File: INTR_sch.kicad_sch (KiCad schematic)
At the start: 6 parts, among them U18 8259A

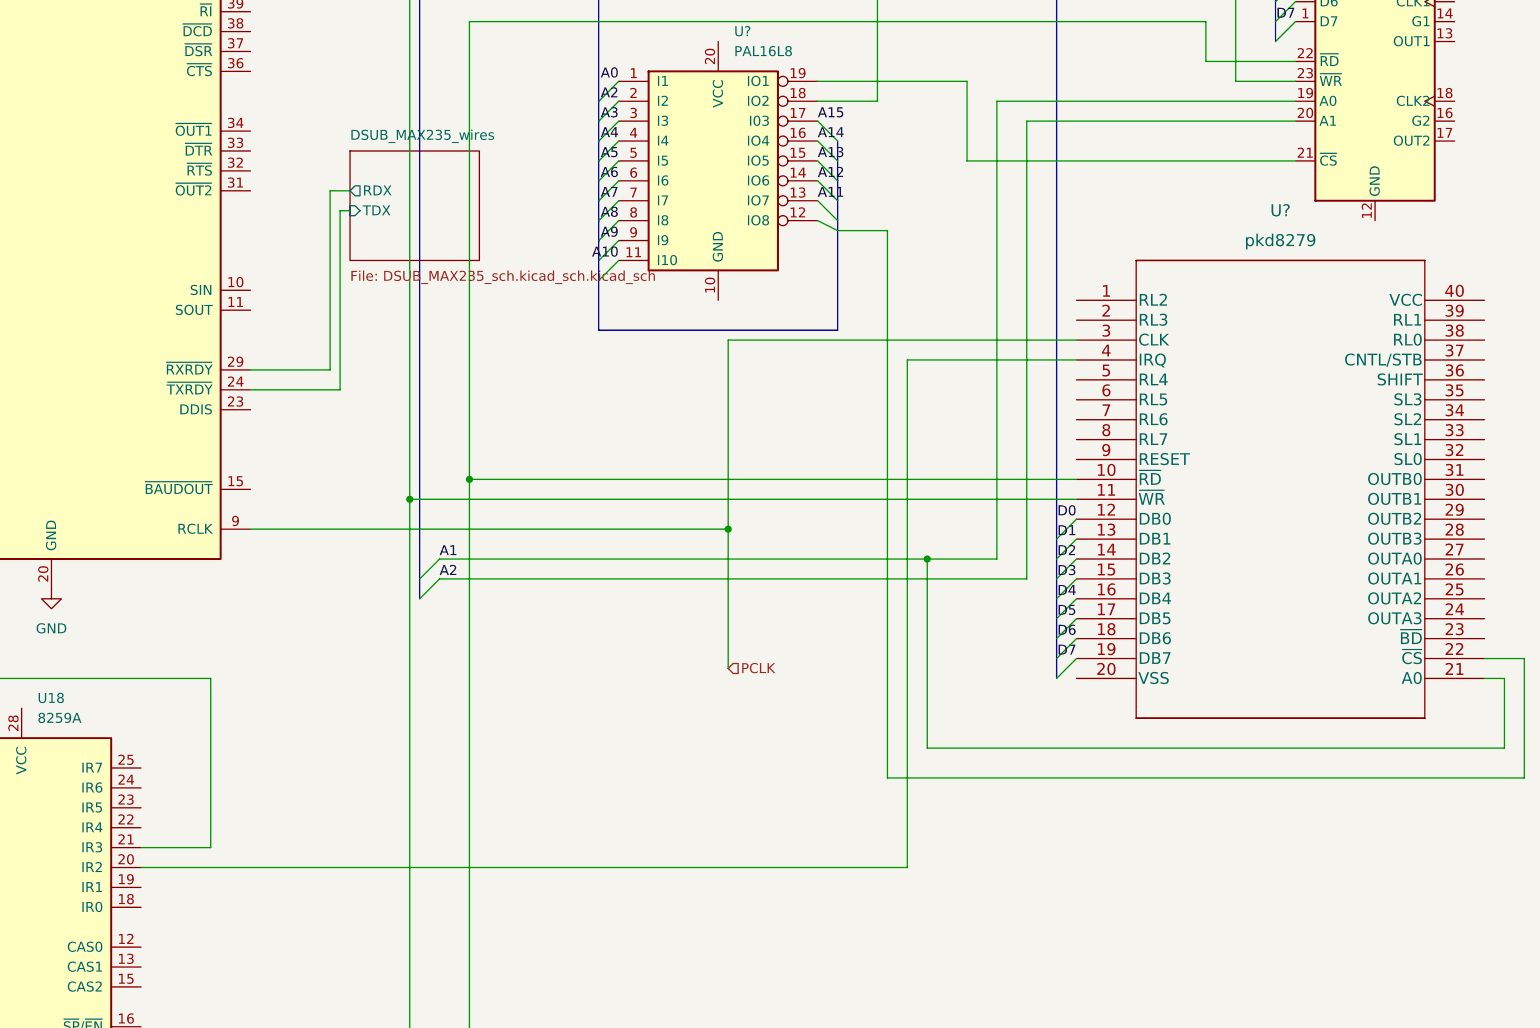
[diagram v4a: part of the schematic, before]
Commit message: Connected 8284 to 8259
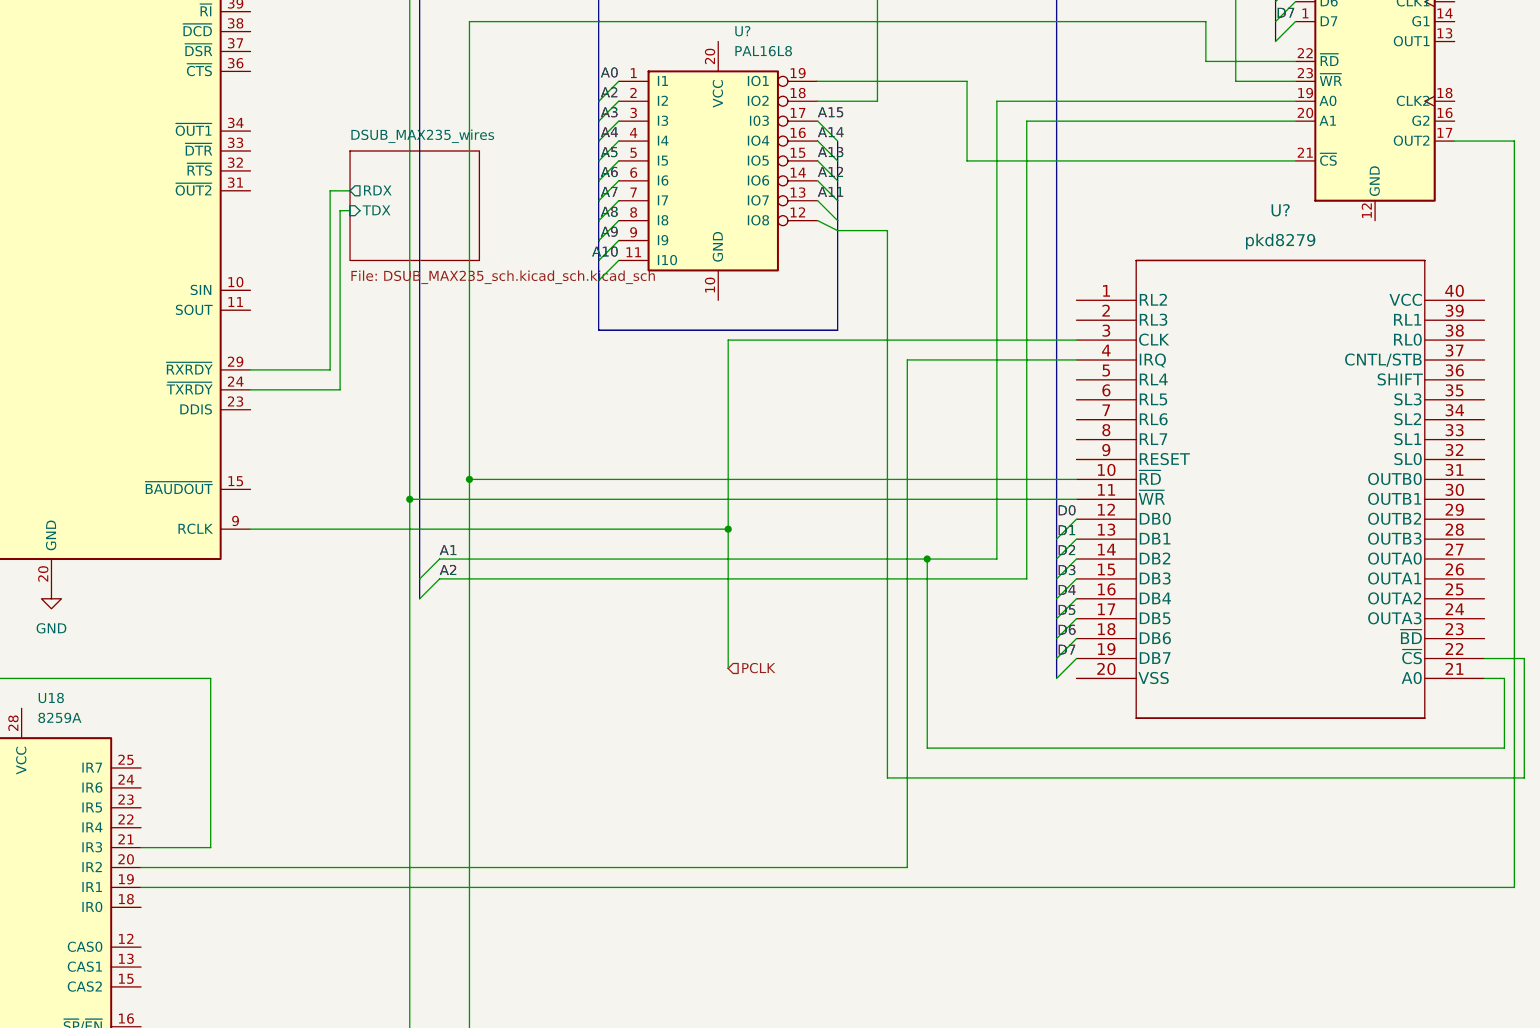
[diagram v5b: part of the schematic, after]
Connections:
- net at U18.19 (IR1): now also U?.17 (OUT2)
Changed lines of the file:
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@@
+    (stroke (width 0) (type default) (color 0 0 0 0))
+  )
+  (wire (pts (xy 281.94 149.86) (xy 106.68 149.86))
     (stroke (width 0) (type default) (color 0 0 0 0))
   )
@@
     (stroke (width 0) (type default) (color 0 0 0 0))
   )
+  (wire (pts (xy 281.94 54.61) (xy 281.94 149.86))
+    (stroke (width 0) (type default) (color 0 0 0 0))
+  )
   (wire (pts (xy 204.47 82.55) (xy 204.47 147.32))
     (stroke (width 0) (type default) (color 0 0 0 0))
@@
     (stroke (width 0) (type default) (color 0 0 0 0))
   )
+  (wire (pts (xy 274.32 54.61) (xy 281.94 54.61))
+    (stroke (width 0) (type default) (color 0 0 0 0))
+  )

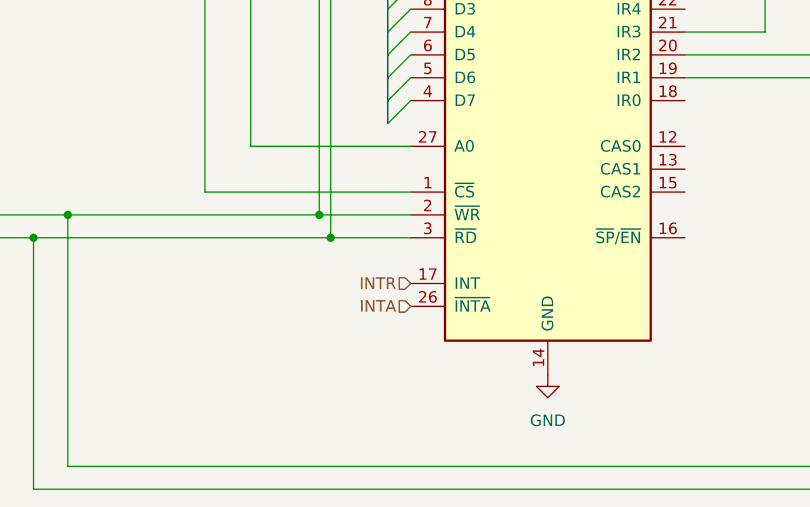
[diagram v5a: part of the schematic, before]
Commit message: Made reset switch for 8284
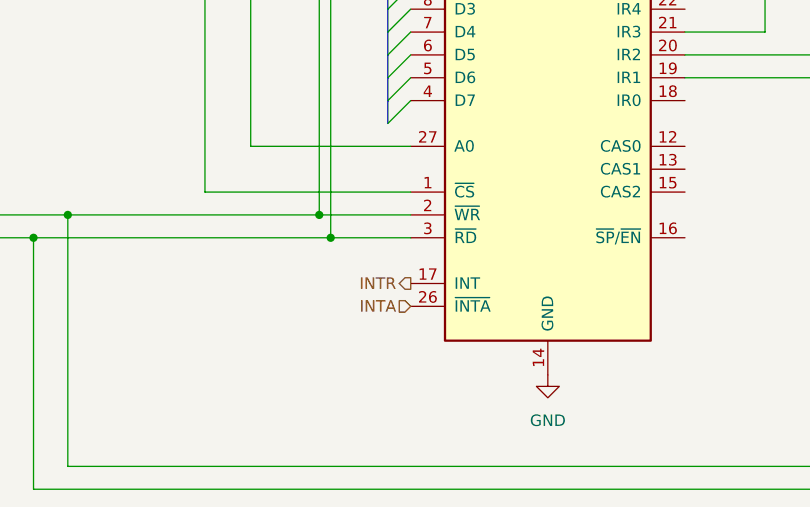
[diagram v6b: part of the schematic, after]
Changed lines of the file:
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@@
     (effects (font (size 1.27 1.27)) (justify right))
   )
-  (hierarchical_label "INTR" (shape input) (at 76.2 172.72 180)
+  (hierarchical_label "INTR" (shape output) (at 76.2 172.72 180)
     (effects (font (size 1.27 1.27)) (justify right))
   )

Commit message: Redid Bus
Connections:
- net M/IO: no longer names the net of U?.13 (IO7), U?.18 (IO2)
- net RD: no longer names the net of U18.3 (~{RD}), U?.10 (~{RD}), U?.21 (~{RD}), U?.22 (~{RD})
- net WR: no longer names the net of U18.2 (~{WR}), U?.11 (~{WR}), U?.18 (~{WR}), U?.23 (~{WR})
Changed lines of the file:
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@@
   (junction (at 64.77 33.02) (diameter 0) (color 0 0 0 0)
   )
+  (junction (at 17.78 36.83) (diameter 0) (color 0 0 0 0)
+  )
   (junction (at 36.83 17.78) (diameter 0) (color 0 0 0 0)
   )
@@
     (stroke (width 0) (type default) (color 0 0 0 0))
   )
+  (bus_entry (at 17.78 165.1) (size 2.54 2.54)
+    (stroke (width 0) (type default) (color 0 0 0 0))
+  )
+  (bus_entry (at 17.78 162.56) (size 2.54 2.54)
+    (stroke (width 0) (type default) (color 0 0 0 0))
+  )
+  (bus_entry (at 21.59 36.83) (size 2.54 2.54)
+    (stroke (width 0) (type default) (color 0 0 0 0))
+  )
   (bus_entry (at 19.05 63.5) (size 2.54 -2.54)
     (stroke (width 0) (type default) (color 0 0 0 0))
@@
     (stroke (width 0) (type default) (color 0 0 0 0))
   )
+  (bus (pts (xy 17.78 162.56) (xy 17.78 165.1))
+    (stroke (width 0) (type default) (color 0 0 0 0))
+  )
   (wire (pts (xy 148.59 195.58) (xy 148.59 97.79))
     (stroke (width 0) (type default) (color 0 0 0 0))
@@
     (stroke (width 0) (type default) (color 0 0 0 0))
   )
-  (wire (pts (xy 25.4 167.64) (xy 34.29 167.64))
+  (wire (pts (xy 20.32 167.64) (xy 34.29 167.64))
     (stroke (width 0) (type default) (color 0 0 0 0))
   )
@@
     (stroke (width 0) (type default) (color 0 0 0 0))
   )
+  (bus (pts (xy 17.78 36.83) (xy 21.59 36.83))
+    (stroke (width 0) (type default) (color 0 0 0 0))
+  )
   (wire (pts (xy 148.59 97.79) (xy 148.59 39.37))
     (stroke (width 0) (type default) (color 0 0 0 0))
@@
     (stroke (width 0) (type default) (color 0 0 0 0))
   )
+  (bus (pts (xy 16.51 36.83) (xy 17.78 36.83))
+    (stroke (width 0) (type default) (color 0 0 0 0))
+  )
   (bus (pts (xy 251.46 26.67) (xy 251.46 29.21))
     (stroke (width 0) (type default) (color 0 0 0 0))
@@
     (stroke (width 0) (type default) (color 0 0 0 0))
   )
-  (wire (pts (xy 25.4 165.1) (xy 38.1 165.1))
-    (stroke (width 0) (type default) (color 0 0 0 0))
-  )
   (wire (pts (xy 120.65 83.82) (xy 130.81 83.82))
     (stroke (width 0) (type default) (color 0 0 0 0))
@@
     (stroke (width 0) (type default) (color 0 0 0 0))
   )
+  (wire (pts (xy 20.32 165.1) (xy 38.1 165.1))
+    (stroke (width 0) (type default) (color 0 0 0 0))
+  )
   (bus (pts (xy 19.05 104.14) (xy 19.05 106.68))
     (stroke (width 0) (type default) (color 0 0 0 0))
   )
+  (bus (pts (xy 17.78 36.83) (xy 17.78 162.56))
+    (stroke (width 0) (type default) (color 0 0 0 0))
+  )
   (wire (pts (xy 246.38 46.99) (xy 254 46.99))
     (stroke (width 0) (type default) (color 0 0 0 0))
@@
   (label "D1" (at 254 24.13 180)
     (effects (font (size 1.27 1.27)) (justify right bottom))
-  )
-  (hierarchical_label "WR" (shape input) (at 25.4 165.1 180)
-    (effects (font (size 1.27 1.27)) (justify right))
   )
   (hierarchical_label "INTR" (shape output) (at 76.2 172.72 180)
@@
     (effects (font (size 1.27 1.27)) (justify right))
   )
-  (hierarchical_label "M{slash}IO" (shape input) (at 24.13 39.37 180)
-    (effects (font (size 1.27 1.27)) (justify right))
-  )
   (hierarchical_label "DataBus" (shape input) (at 24.13 33.02 180)
     (effects (font (size 1.27 1.27)) (justify right))
   )
+  (hierarchical_label "ControlBus" (shape input) (at 16.51 36.83 180)
+    (effects (font (size 1.27 1.27)) (justify right))
+  )
   (hierarchical_label "Reset" (shape input) (at 24.13 41.91 180)
     (effects (font (size 1.27 1.27)) (justify right))
@@
     (effects (font (size 1.27 1.27)) (justify left))
   )
-  (hierarchical_label "RD" (shape input) (at 25.4 167.64 180)
-    (effects (font (size 1.27 1.27)) (justify right))
-  )
   (hierarchical_label "INTA" (shape input) (at 76.2 175.26 180)
